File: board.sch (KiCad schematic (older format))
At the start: 14 parts, among them J1 B2B-PH-K-S_LF__SN_, J2 B2B-PH-K-S_LF__SN_, J3 B2B-PH-K-S_LF__SN_, J4 B2B-PH-K-S_LF__SN_, J5 B2B-PH-K-S_LF__SN_, J6 B2B-PH-K-S_LF__SN_, J7 Conn_01x02, J8 B7B-XH-A_LF__SN_

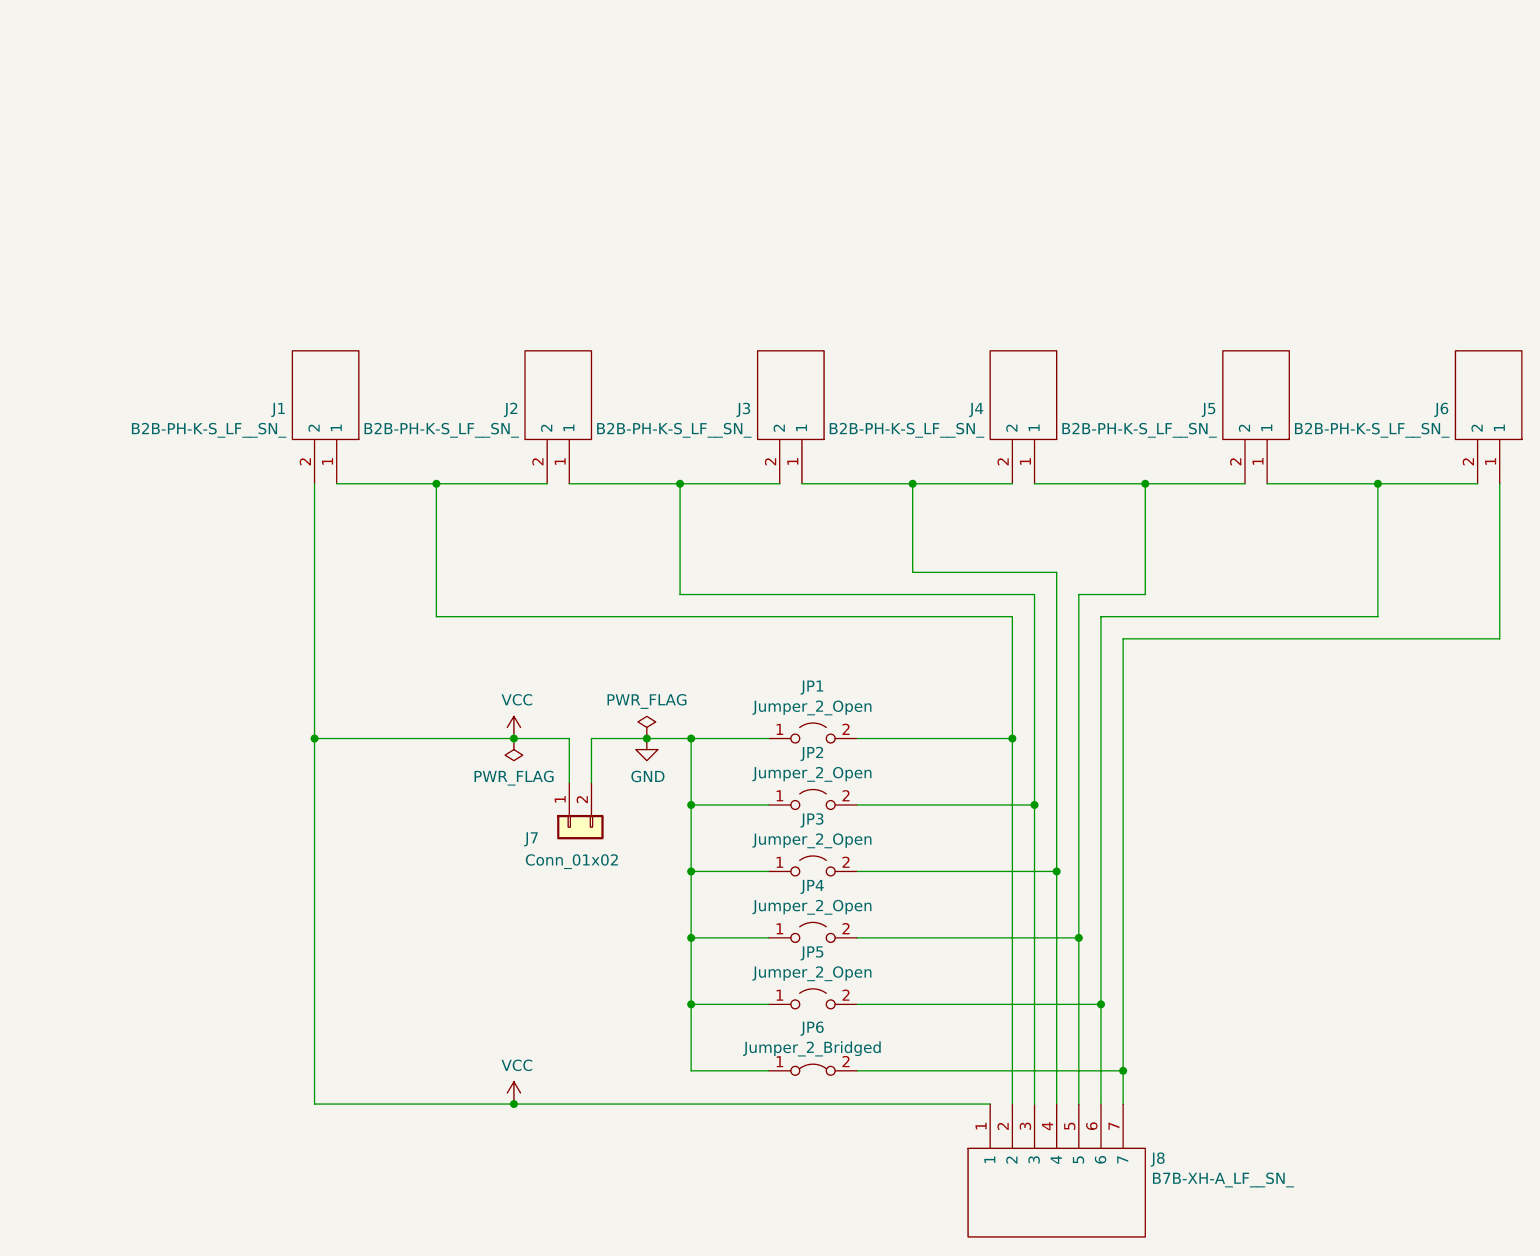
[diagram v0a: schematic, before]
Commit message: New 1s, 2s and 3s design.
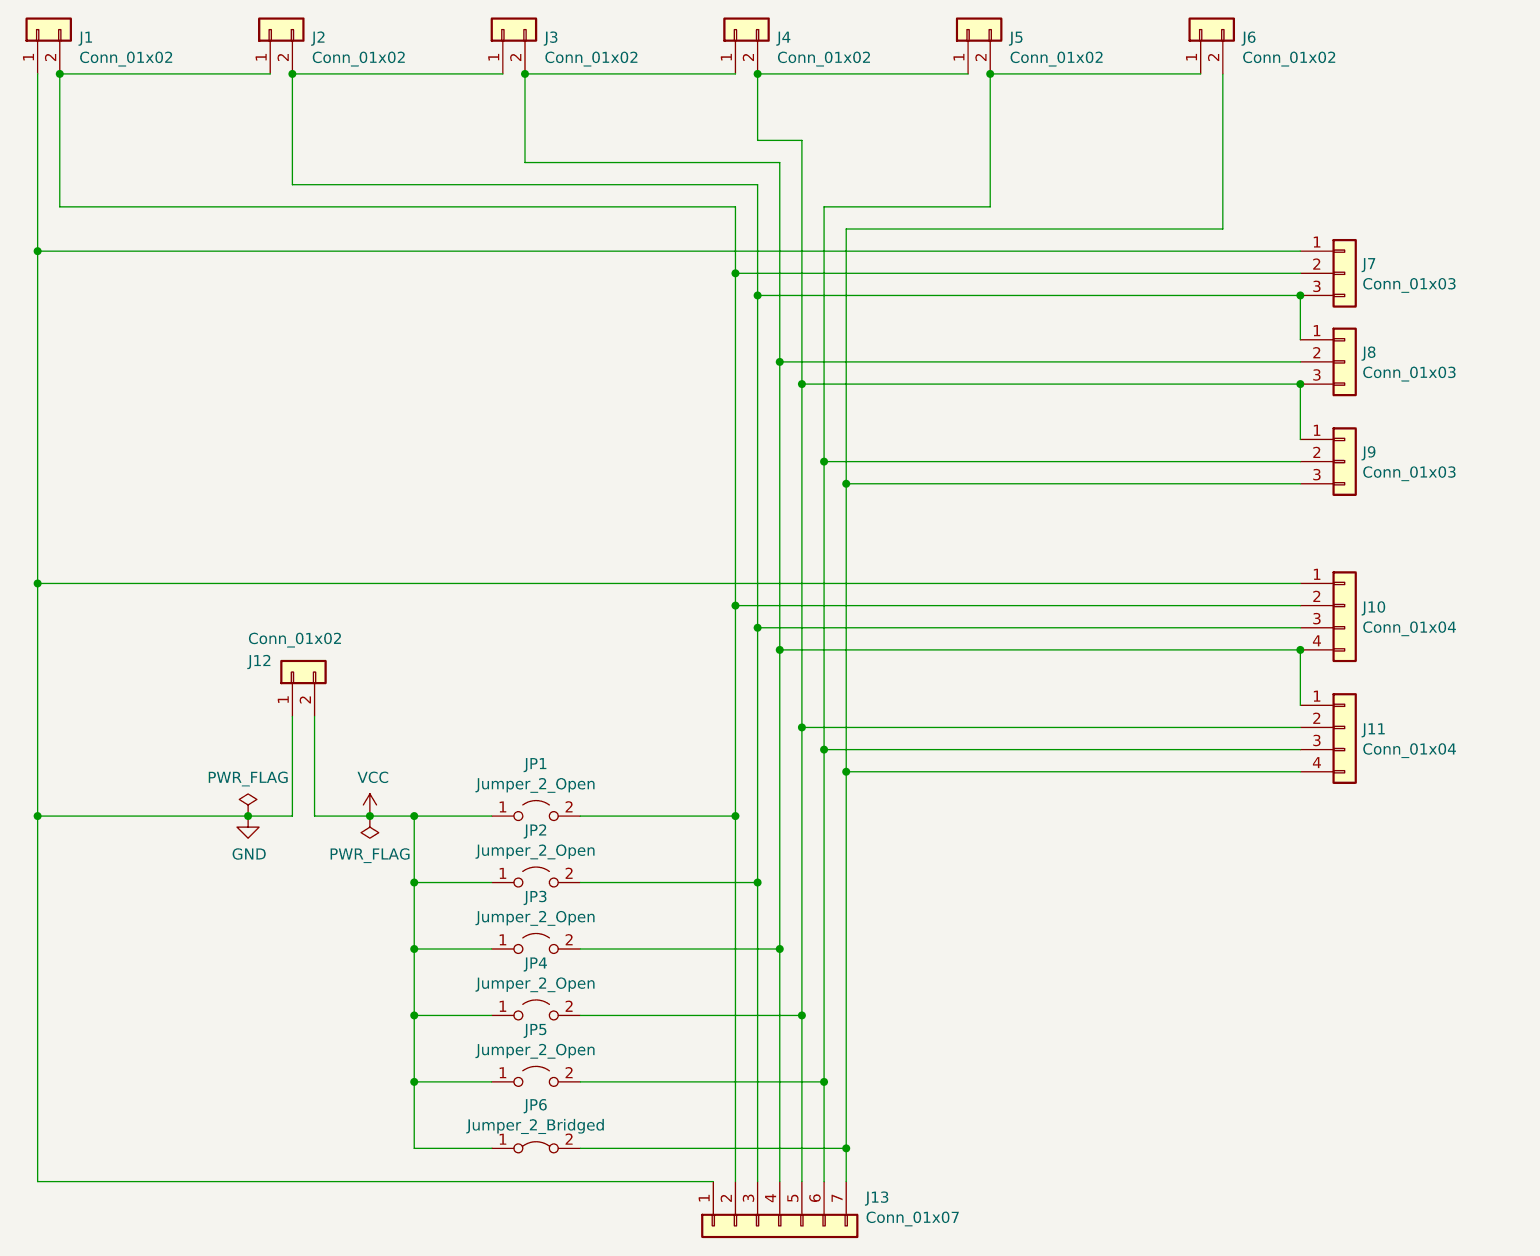
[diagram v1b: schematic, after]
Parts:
- removed J1, J2, J3, J4, J5, J6: B2B-PH-K-S_LF__SN_, Connector_JST:JST_PH_B2B-PH-K_1x02_P2.00mm_Vertical, symbol SamacSys_Parts:B2B-PH-K-S_LF__SN_
- removed J8: B7B-XH-A_LF__SN_, Connector_JST:JST_XH_B7B-XH-A_1x07_P2.50mm_Vertical, symbol SamacSys_Parts:B7B-XH-A_LF__SN_
- added J1, J2, J3, J4, J5, J6: Conn_01x02, Connector_JST:JST_PH_B2B-PH-K_1x02_P2.00mm_Vertical, symbol Connector_Generic:Conn_01x02
- added J10, J11: Conn_01x04, Connector_JST:JST_XH_B4B-XH-A_1x04_P2.50mm_Vertical, symbol Connector_Generic:Conn_01x04
- added J13: Conn_01x07, Connector_JST:JST_XH_B7B-XH-A_1x07_P2.50mm_Vertical, symbol Connector_Generic:Conn_01x07
- added J7, J8, J9: Conn_01x03, Connector_JST:JST_XH_B3B-XH-A_1x03_P2.50mm_Vertical, symbol Connector_Generic:Conn_01x03
- renumbered J7 to J12
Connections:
- net GND: now also J12.1 (Pin_1), J1.1 (Pin_1), J10.1 (Pin_1), J13.1 (Pin_1), J7.1 (Pin_1); no longer J12.2 (Pin_2), JP1.1 (A), JP2.1 (A), JP3.1 (A), JP4.1 (A), JP5.1 (A), JP6.1 (A)
- net VCC: now also J12.2 (Pin_2), JP1.1 (A), JP2.1 (A), JP3.1 (A), JP4.1 (A), JP5.1 (A), JP6.1 (A); no longer J12.1 (Pin_1)
- net at JP1.2 (B): now also J1.2 (Pin_2), J10.2 (Pin_2), J13.2 (Pin_2), J2.1 (Pin_1), J7.2 (Pin_2)
- net at JP2.2 (B): now also J10.3 (Pin_3), J13.3 (Pin_3), J2.2 (Pin_2), J3.1 (Pin_1), J7.3 (Pin_3), J8.1 (Pin_1)
- net at JP3.2 (B): now also J10.4 (Pin_4), J11.1 (Pin_1), J13.4 (Pin_4), J3.2 (Pin_2), J4.1 (Pin_1), J8.2 (Pin_2)
- net at JP4.2 (B): now also J11.2 (Pin_2), J13.5 (Pin_5), J4.2 (Pin_2), J5.1 (Pin_1), J8.3 (Pin_3), J9.1 (Pin_1)
- net at JP5.2 (B): now also J11.3 (Pin_3), J13.6 (Pin_6), J5.2 (Pin_2), J6.1 (Pin_1), J9.2 (Pin_2)
- net at JP6.2 (B): now also J11.4 (Pin_4), J13.7 (Pin_7), J6.2 (Pin_2), J9.3 (Pin_3)
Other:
- moved on the sheet: J12, JP1, JP2, JP3, JP4, JP5, JP6
